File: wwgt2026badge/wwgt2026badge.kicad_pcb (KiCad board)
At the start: 2 copper layers, 100 x 70 mm, 19 parts, among them J1 Conn_01x08_Pin, J2 Conn_01x04_Pin, SW1 SW_PUSH, SW2 EC12PLGRSDVF, SW2 KEY_SWITCH, SW3 SW_PUSH, U2 rp2040-zero, U3 fj08k-s

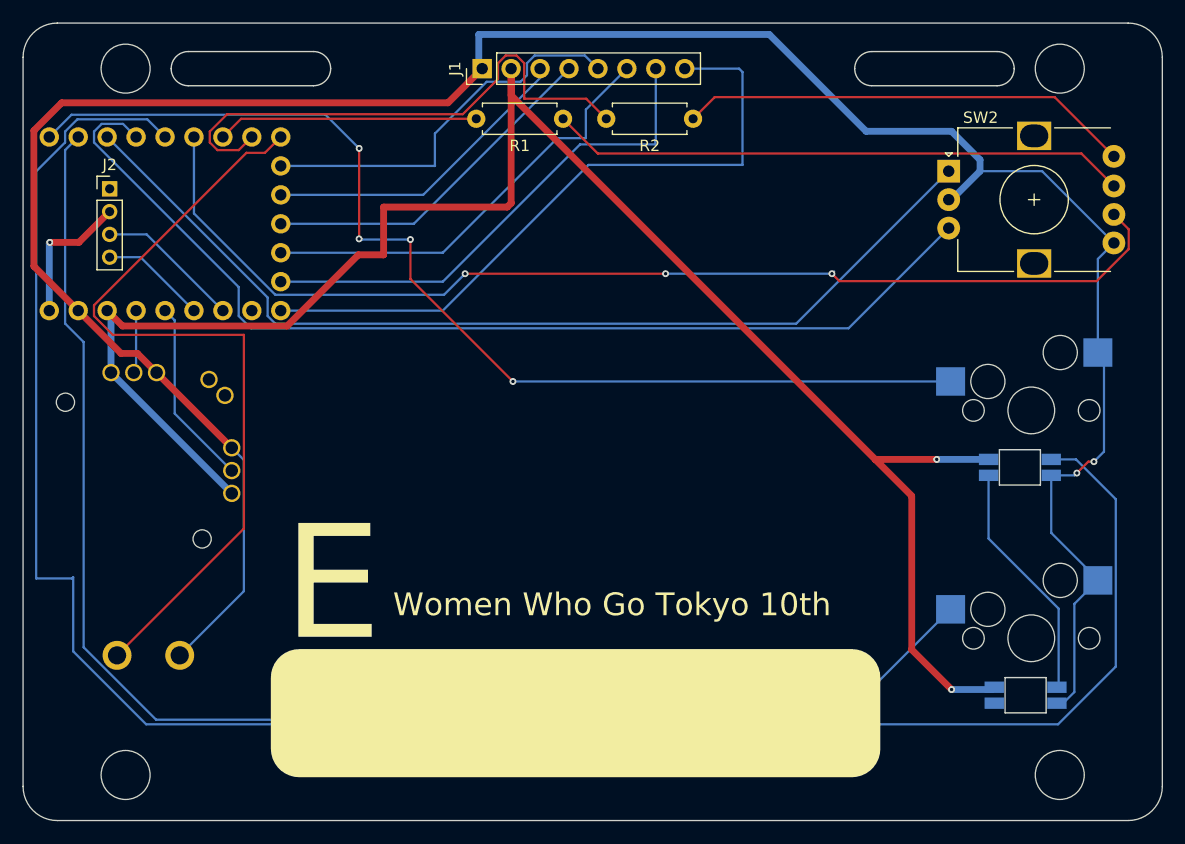
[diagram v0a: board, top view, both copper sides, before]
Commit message: エンコーダーのフットプリントを修正 + 回路およびPCBのエラーを修正
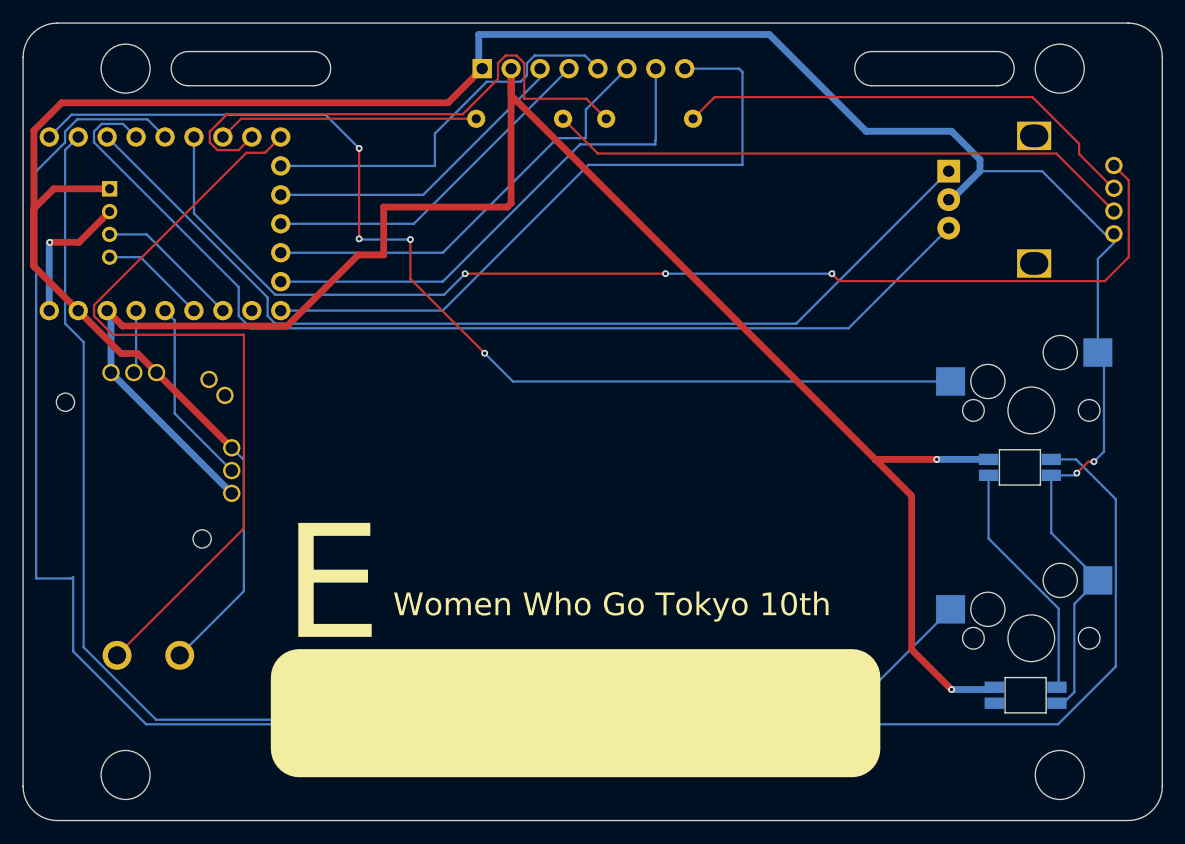
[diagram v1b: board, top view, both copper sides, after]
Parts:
- removed the SW2 at (50.0, 24.0)
- removed the SW2 at (110.0, 24.0)
- added H5: MountingHole, foostan/kbd:M2_HOLE_v2, F.Cu at (50.0, 24.0)
- added H6: MountingHole, foostan/kbd:M2_HOLE_v2, F.Cu at (110.0, 24.0)
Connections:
- R1 pad 1: Net-(R1-Pad1) -> Net-(SW2-LED1)
- R2 pad 1: Net-(R2-Pad1) -> Net-(SW2-LED2)
- SW2 pad 2: ENC_BTN -> Net-(SW2-LED1)
- SW2 pad 3: Net-(R1-Pad1) -> Net-(SW2-LED2)
- SW2 pad 4: Net-(R2-Pad1) -> ENC_BTN
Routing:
- net Net-(R1-Pad1): track 52.6 -> 0.00 mm
- net Net-(SW2-LED1): track 0.00 -> 51.7 mm
- net Net-(SW2-LED2): track 0.00 -> 41.6 mm
- net Net-(R2-Pad1): track 39.9 -> 0.00 mm
- net GND: track 218.4 -> 230.8 mm
- net ENC_BTN: track 97.8 -> 102.5 mm

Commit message: QR コードを追加
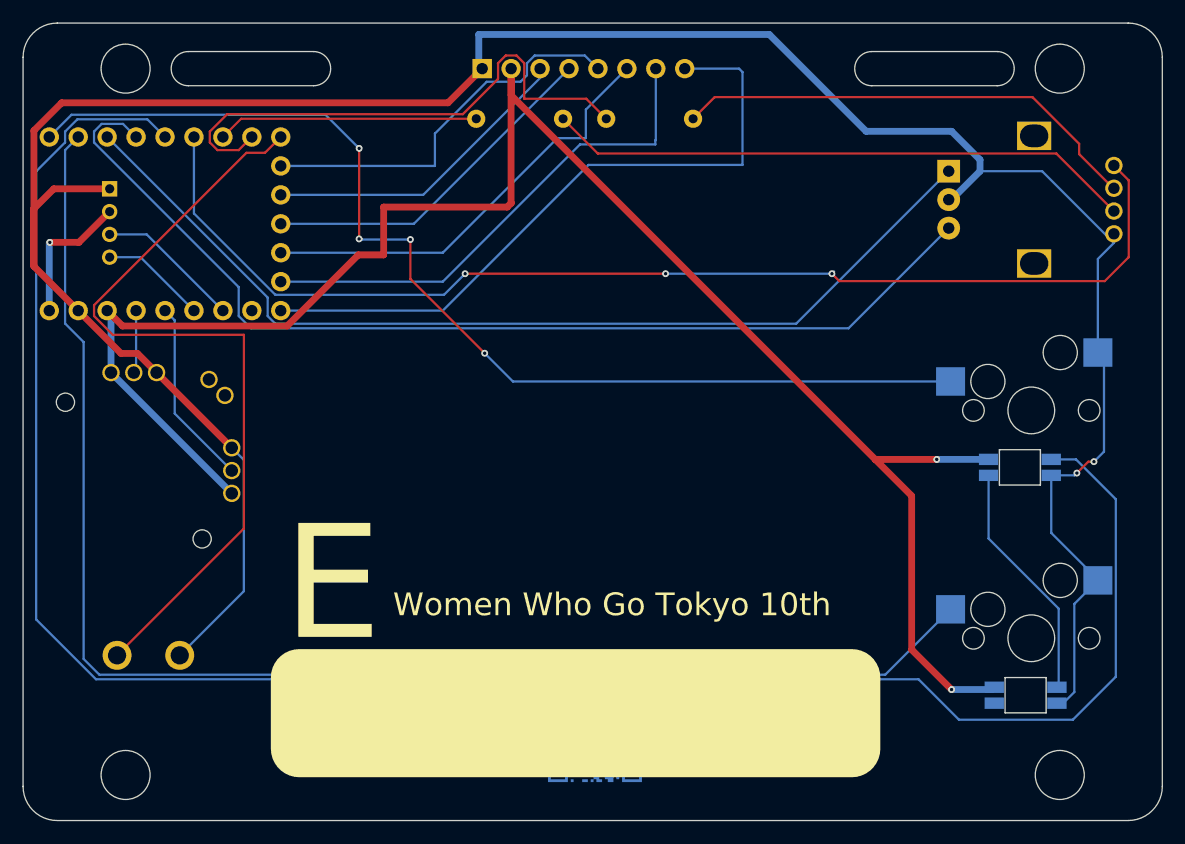
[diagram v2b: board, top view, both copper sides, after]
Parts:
- added QR*****: https://github.com/WomenWhoGoTokyo/2026-anniversary-badge, sglib:QR wwgt-2026-anniversary-badge, B.Cu at (80.2, 82.5)
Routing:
- net SW_1: track 128.7 -> 126.0 mm
- net SK6812MINI-E: track 178.0 -> 176.4 mm

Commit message: テスト用に QR コードを追加
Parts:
- removed the QR***** at (80.2, 82.5)
- added QR*****: https://github.com/WomenWhoGoTokyo/2026-anniversary-badge, sglib:qr-0.5, F.Cu at (80.0, 60.0)
- added qr-0.25: https://github.com/WomenWhoGoTokyo/2026-anniversary-badge, sglib:qr-0.25, B.Cu at (100.0, 81.0)
- added qr-0.3: https://github.com/WomenWhoGoTokyo/2026-anniversary-badge, sglib:qr-0.3, B.Cu at (87.0, 81.0)
- added qr-0.35: https://github.com/WomenWhoGoTokyo/2026-anniversary-badge, sglib:qr-0.35, B.Cu at (72.0, 81.0)
- added qr-0.4: https://github.com/WomenWhoGoTokyo/2026-anniversary-badge, sglib:qr-0.4, B.Cu at (56.0, 82.0)
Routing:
- net SK6812MINI-E: track 176.4 -> 179.4 mm
- net SW_1: track 126.0 -> 128.0 mm

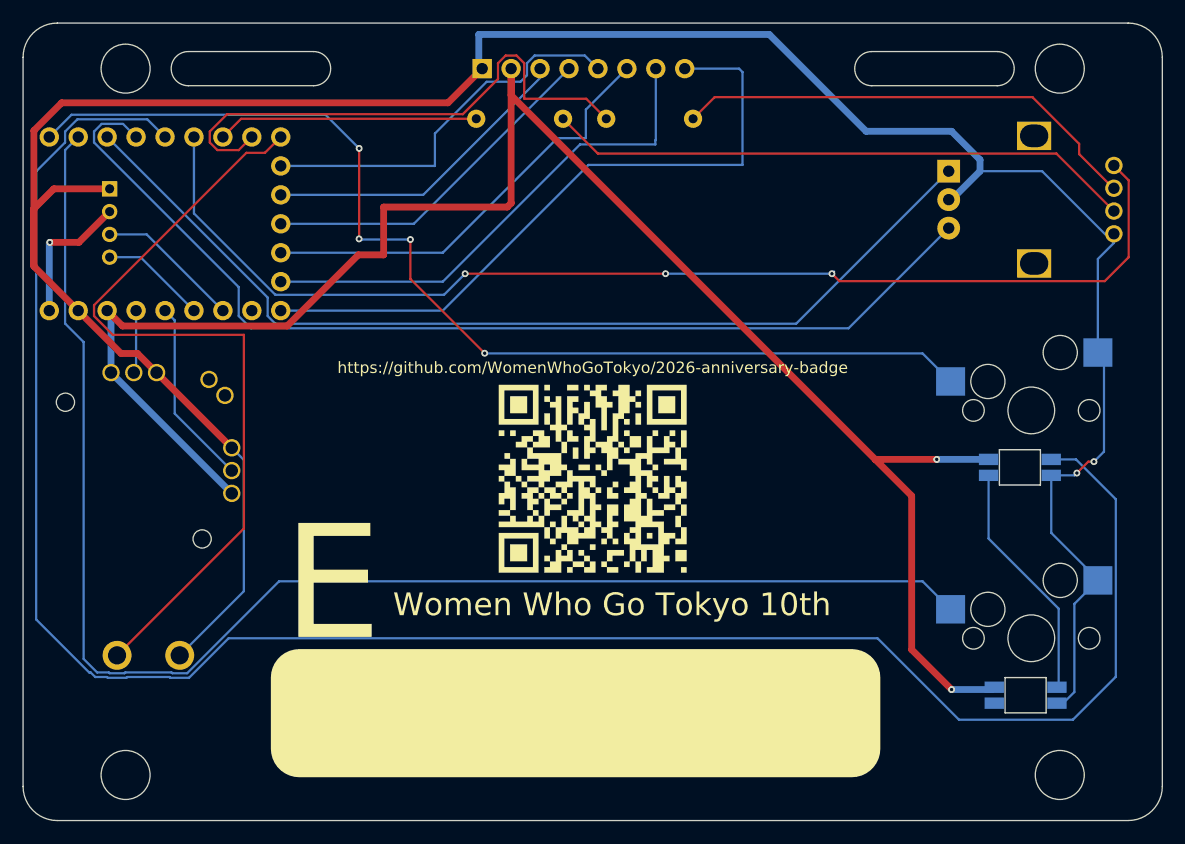
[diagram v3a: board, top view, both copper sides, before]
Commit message: Grove端子の位置を調整してベタGNDを追加
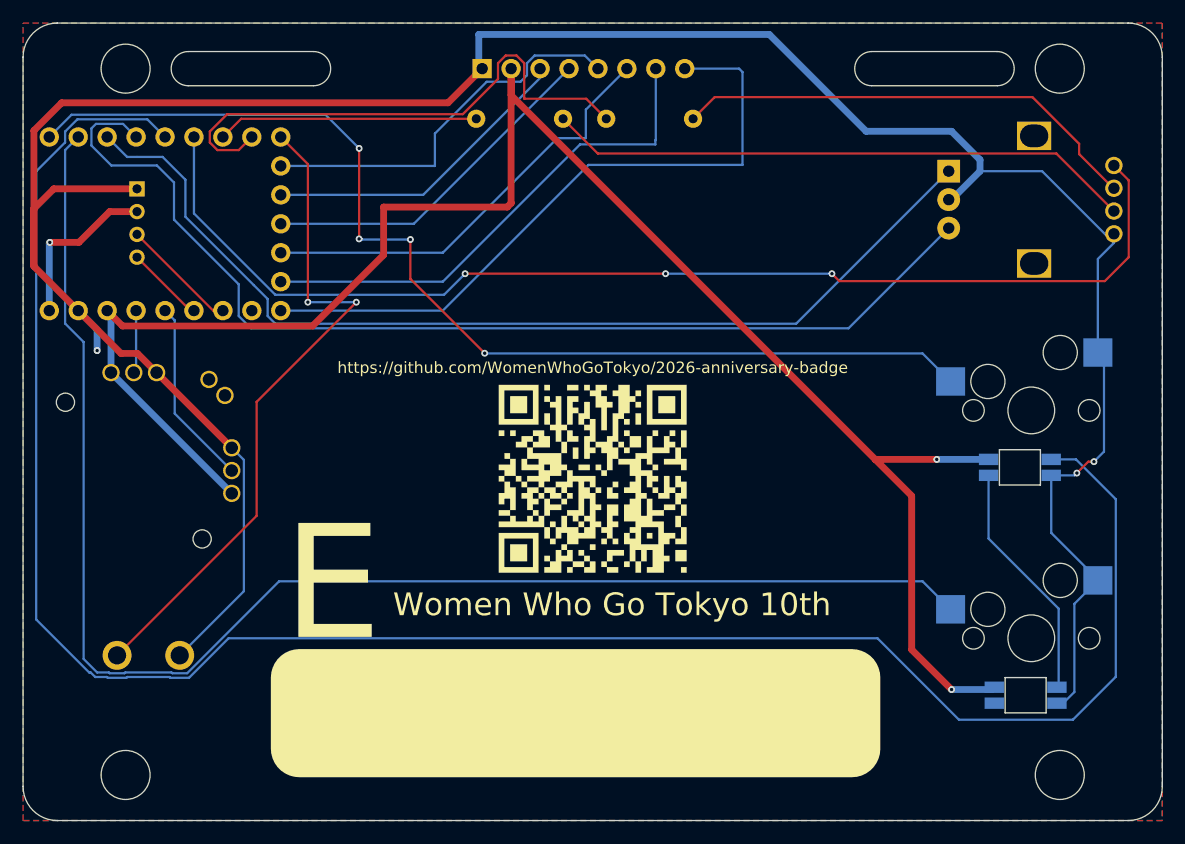
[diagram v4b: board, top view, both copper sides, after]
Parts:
- moved J2 2.40 mm to (40.0, 34.5)
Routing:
- net BUZZER: track 70.2 -> 59.6 mm, vias 0 -> 2
- net GND: track 230.8 -> 237.4 mm, vias 2 -> 3
- net ROT_B: track 92.3 -> 95.1 mm
- net VCC: track 12.4 -> 14.8 mm
- net /SDA1: track 12.3 -> 10.3 mm
- net /SCL1: track 8.94 -> 6.94 mm
- net ROT_A: track 87.2 -> 89.0 mm
- added copper zone on B.Cu, net GND
- added copper zone on F.Cu, net GND

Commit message: updated gopher font & gerbar files
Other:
- board text added: "JZV"
- board text removed: "FAE"

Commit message: fixed pcb file
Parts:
- removed qr-0.25: https://github.com/WomenWhoGoTokyo/2026-anniversary-badge, sglib:qr-0.25
- removed qr-0.3: https://github.com/WomenWhoGoTokyo/2026-anniversary-badge, sglib:qr-0.3
- removed qr-0.35: https://github.com/WomenWhoGoTokyo/2026-anniversary-badge, sglib:qr-0.35
- moved qr-0.4 25.3 mm to (80.6, 76.2)
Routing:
- net SW_1: track 128.0 -> 133.7 mm
- net SK6812MINI-E: track 179.4 -> 181.3 mm

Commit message: fixed pcb file (front)
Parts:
- removed QR*****: https://github.com/WomenWhoGoTokyo/2026-anniversary-badge, sglib:qr-0.5

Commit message: fixed pcb file
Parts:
- moved J1 1.25 mm to (71.5, 24.0)
- moved R1 1.25 mm to (78.7, 28.4)
- moved R2 1.25 mm to (90.1, 28.4)
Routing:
- net GND: track 237.4 -> 262.8 mm, vias 3 -> 4
- net DC: track 38.5 -> 57.1 mm
- net CS: track 44.5 -> 57.4 mm
- net SCL: track 27.8 -> 40.6 mm
- net SDA: track 30.9 -> 40.0 mm
- net ENC_LED_2: track 47.9 -> 40.6 mm
- net 3V3: track 160.2 -> 153.4 mm
- net RES: track 34.6 -> 40.7 mm
- net ENC_LED_1: track 22.9 -> 25.5 mm
- net Net-(SW2-LED2): track 41.6 -> 40.4 mm
- net Net-(SW2-LED1): track 51.7 -> 52.8 mm
